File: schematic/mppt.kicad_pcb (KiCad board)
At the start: 2 copper layers, 25 parts, among them J1 Solar, J10 ACS712-OUT, J11 LiIon-36V, J12 Download, J2 TL494-IN, J3 LM2596-IN, J4 LM2596-IN, J5 Serial, J6 LM2596-OUT-4,5V, J7 LM2596-OUT-3,3V, J8 ACS712-IN, J9 TL494-OUT-42V-3A, U3 ESP-03, U4 74HC4051

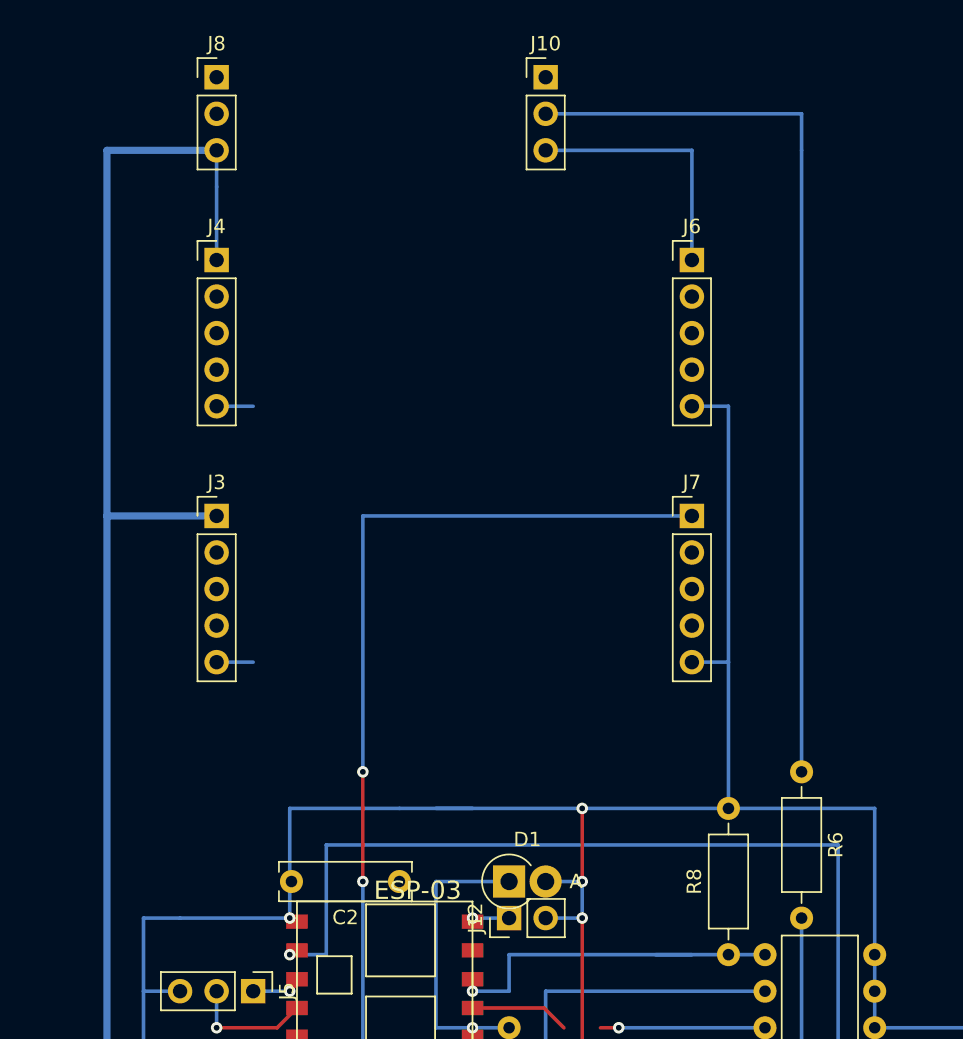
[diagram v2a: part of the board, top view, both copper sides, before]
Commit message: schematic: Use INA219
Signed-off-by: Timo Wischer <twischer@freenet.de>
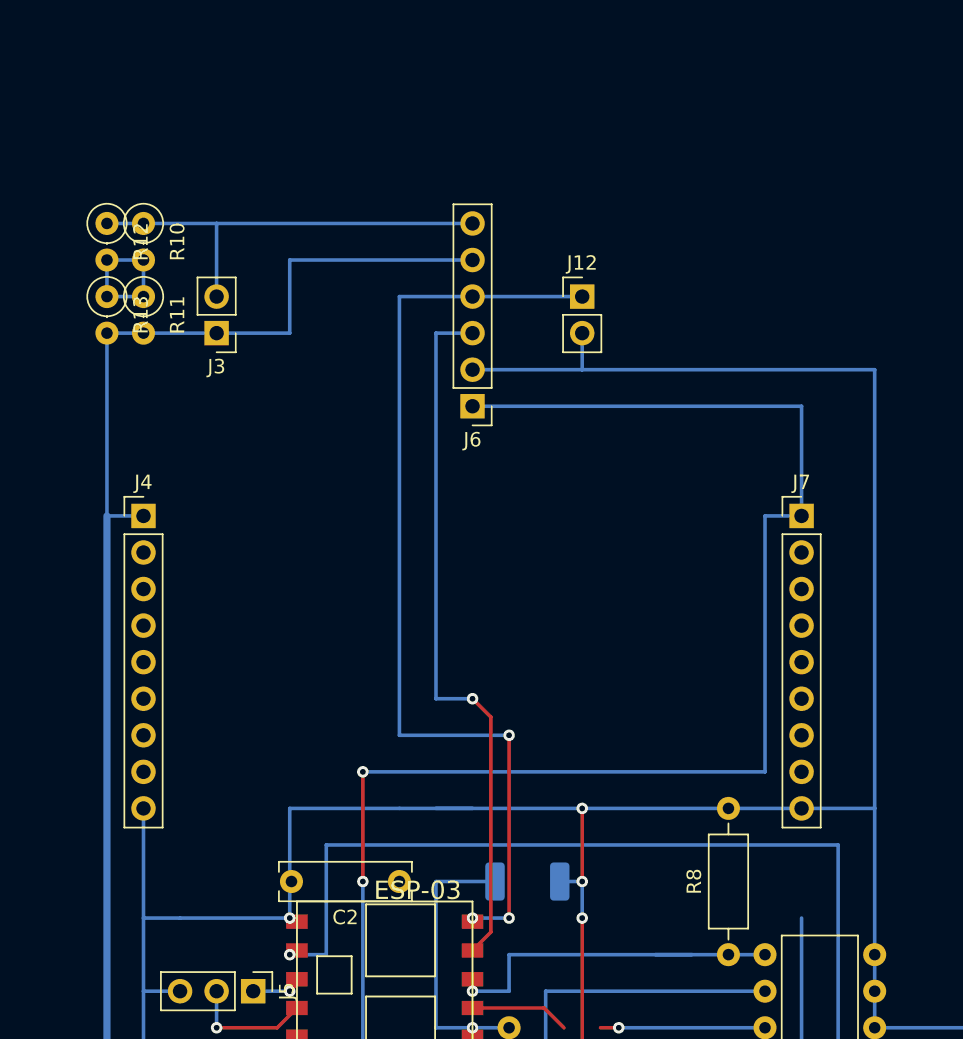
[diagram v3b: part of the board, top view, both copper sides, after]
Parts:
- removed J10: ACS712-OUT, Connector_PinHeader_2.54mm:PinHeader_1x03_P2.54mm_Vertical
- removed J8: ACS712-IN, Connector_PinHeader_2.54mm:PinHeader_1x03_P2.54mm_Vertical
- removed R6: 5k6, Resistor_THT:R_Axial_DIN0207_L6.3mm_D2.5mm_P10.16mm_Horizontal
- added R10: 0,005, Resistor_THT:R_Axial_DIN0207_L6.3mm_D2.5mm_P2.54mm_Vertical, F.Cu at (55.9, 71.1)
- added R11: 0,005, Resistor_THT:R_Axial_DIN0207_L6.3mm_D2.5mm_P2.54mm_Vertical, F.Cu at (55.9, 76.2)
- added R12: 0,005, Resistor_THT:R_Axial_DIN0207_L6.3mm_D2.5mm_P2.54mm_Vertical, F.Cu at (53.3, 71.1)
- added R13: 0,005, Resistor_THT:R_Axial_DIN0207_L6.3mm_D2.5mm_P2.54mm_Vertical, F.Cu at (53.3, 76.2)
- D1: footprint Diode_THT:D_DO-15_P2.54mm_Vertical_AnodeUp -> Diode_SMD:D_2010_5025Metric; moved to B.Cu
- J3: value LM2596-IN -> INA219; footprint Connector_PinHeader_2.54mm:PinHeader_1x05_P2.54mm_Vertical -> Connector_PinHeader_2.54mm:PinHeader_1x02_P2.54mm_Vertical
- J4: footprint Connector_PinHeader_2.54mm:PinHeader_1x05_P2.54mm_Vertical -> Connector_PinHeader_2.54mm:PinHeader_1x09_P2.54mm_Vertical
- J6: value LM2596-OUT-4,5V -> INA219; footprint Connector_PinHeader_2.54mm:PinHeader_1x05_P2.54mm_Vertical -> Connector_PinHeader_2.54mm:PinHeader_1x06_P2.54mm_Vertical
- J7: value LM2596-OUT-3,3V -> LM2596-OUT; footprint Connector_PinHeader_2.54mm:PinHeader_1x05_P2.54mm_Vertical -> Connector_PinHeader_2.54mm:PinHeader_1x09_P2.54mm_Vertical
- moved J12 43.5 mm to (86.4, 76.2), turned to 0 degrees
- moved J4 18.5 mm to (55.9, 91.4)
- moved J6 18.3 mm to (78.7, 83.8), turned to 180 degrees
- moved J3 12.7 mm to (61.0, 78.7), turned to 180 degrees
- moved J7 7.62 mm to (101.6, 91.4)
- moved D1 1.27 mm to (82.5, 116.8)
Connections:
- J3 pad 2: (no net) -> Net-(J1-Pad2)
- J4 pad 5: GND -> (no net)
- J6 pad 1: Net-(J10-Pad3) -> Net-(C2-Pad1)
- J6 pad 2: (no net) -> GND
- J6 pad 3: (no net) -> Net-(J6-Pad3)
- J6 pad 4: (no net) -> Net-(J12-Pad1)
- J6 pad 5: GND -> Net-(J2-Pad1)
- J7 pad 5: GND -> (no net)
- U3 pad 13: (no net) -> Net-(J6-Pad3)
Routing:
- net Net-(J12-Pad1): track 2.79 -> 66.3 mm, vias 1 -> 3
- net Net-(J10-Pad2): track 63.5 -> 0.00 mm
- net Net-(J6-Pad3): track 0.00 -> 49.0 mm, vias 0 -> 1
- net Net-(C2-Pad1): track 112.8 -> 150.9 mm
- net Net-(J1-Pad2): track 0.00 -> 30.5 mm
- net GND: track 239.5 -> 266.4 mm
- net Net-(J10-Pad3): track 17.8 -> 0.00 mm
- net Net-(R10-Pad2): track 0.00 -> 10.2 mm
- net Net-(J2-Pad1): track 172.7 -> 165.1 mm
- net Net-(D1-Pad1): track 20.9 -> 20.0 mm

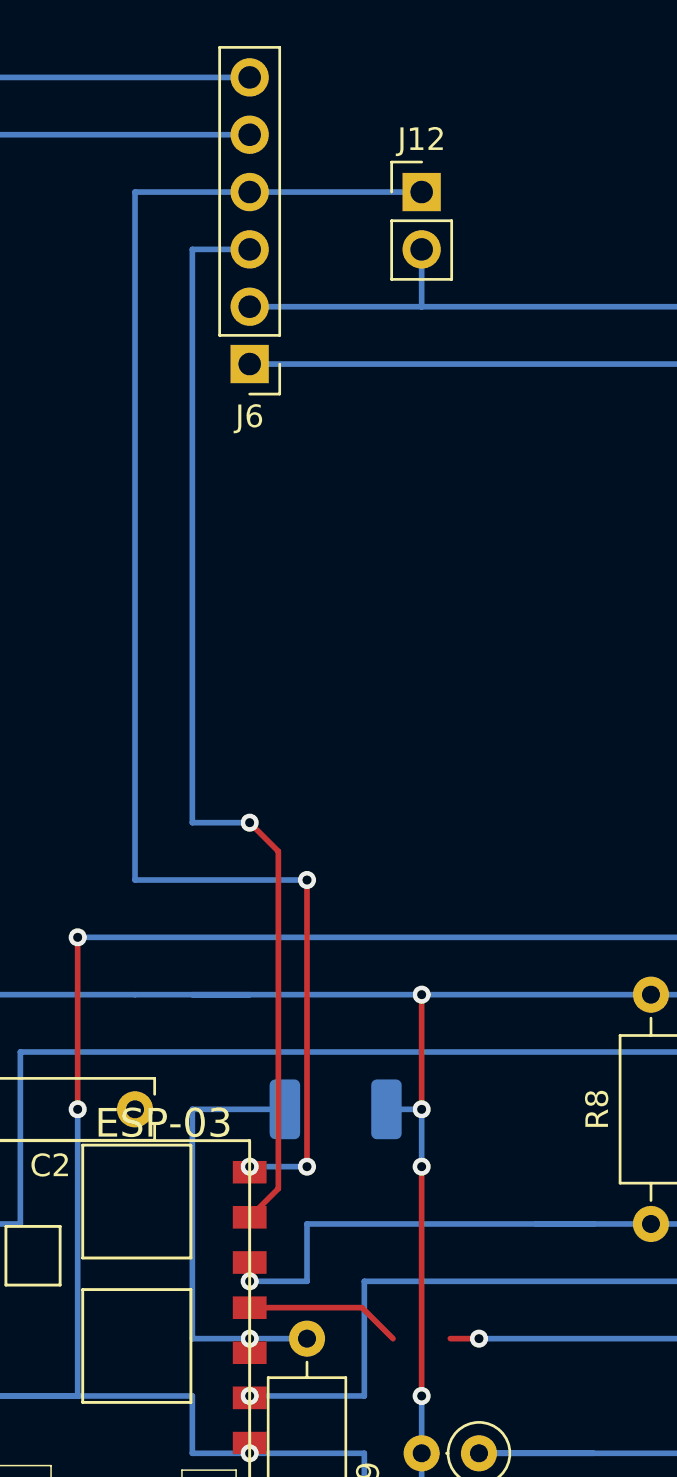
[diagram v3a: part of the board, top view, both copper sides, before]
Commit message: Swap GPIO0 and GPIO13
Signed-off-by: Timo Wischer <twischer@freenet.de>
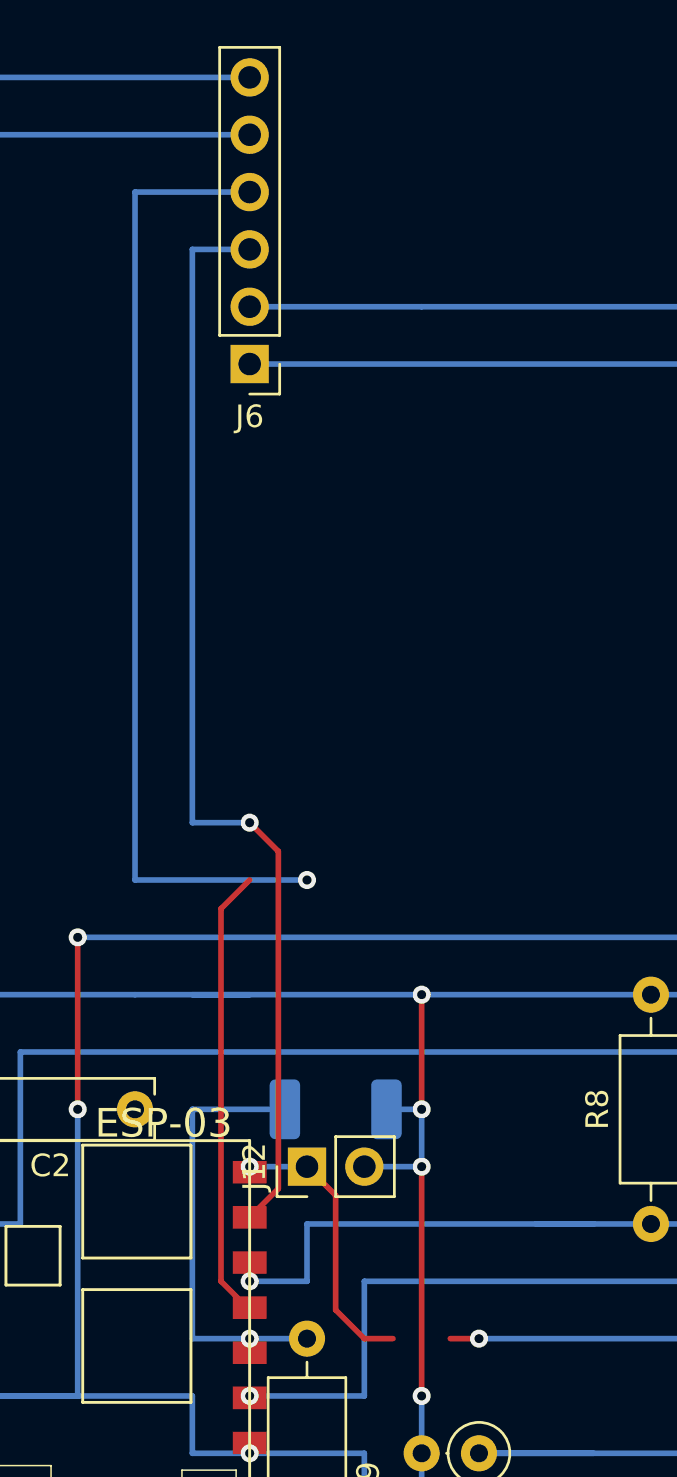
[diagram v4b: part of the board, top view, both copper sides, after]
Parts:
- moved J12 43.5 mm to (81.3, 119.4), turned to 90 degrees
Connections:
- J6 pad 4: Net-(J12-Pad1) -> Net-(J6-Pad4)
- U3 pad 11: Net-(U3-Pad11) -> Net-(J6-Pad4)
- U4 pad 11: Net-(U3-Pad11) -> Net-(J12-Pad1)
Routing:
- net Net-(J6-Pad4): track 0.00 -> 63.2 mm, vias 0 -> 1
- net Net-(J12-Pad1): track 66.3 -> 24.2 mm, vias 3 -> 2
- net Net-(U3-Pad11): track 18.3 -> 0.00 mm, vias 1 -> 0

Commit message: schematic: Reduce GPIO15 pull down to 2,2kOhm
Signed-off-by: Timo Wischer <twischer@freenet.de>
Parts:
- R8: value 10k -> 2k2
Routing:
- net Net-(C1-Pad2): track 0.00 -> 2.54 mm
- net (no net): track 2.54 -> 0.00 mm

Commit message: Update to KiCad 6.0
Signed-off-by: Timo Wischer <twischer@freenet.de>
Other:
- net class Default removed

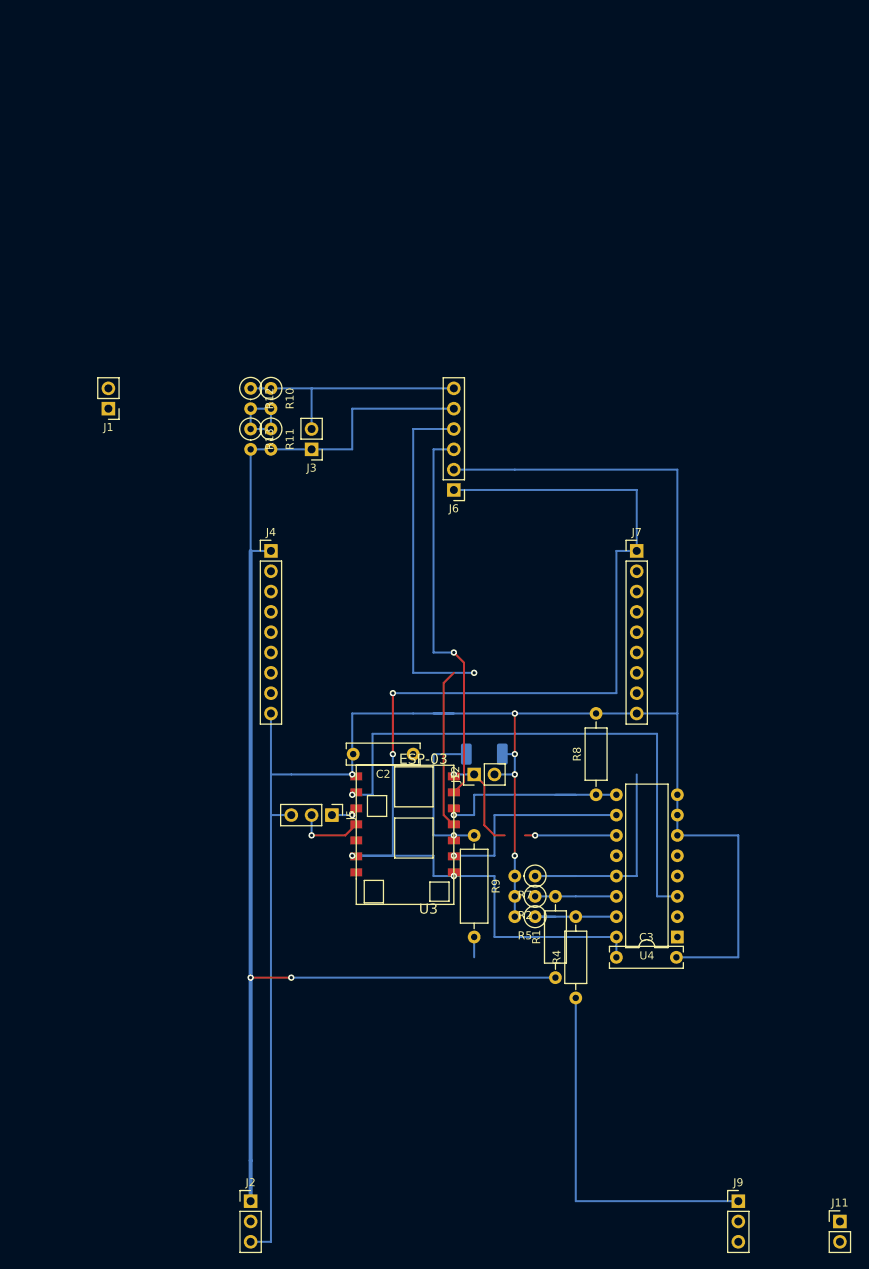
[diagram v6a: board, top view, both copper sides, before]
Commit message: sch: Use error amp of TL494 for MPPT
Signed-off-by: Timo Wischer <twischer@freenet.de>
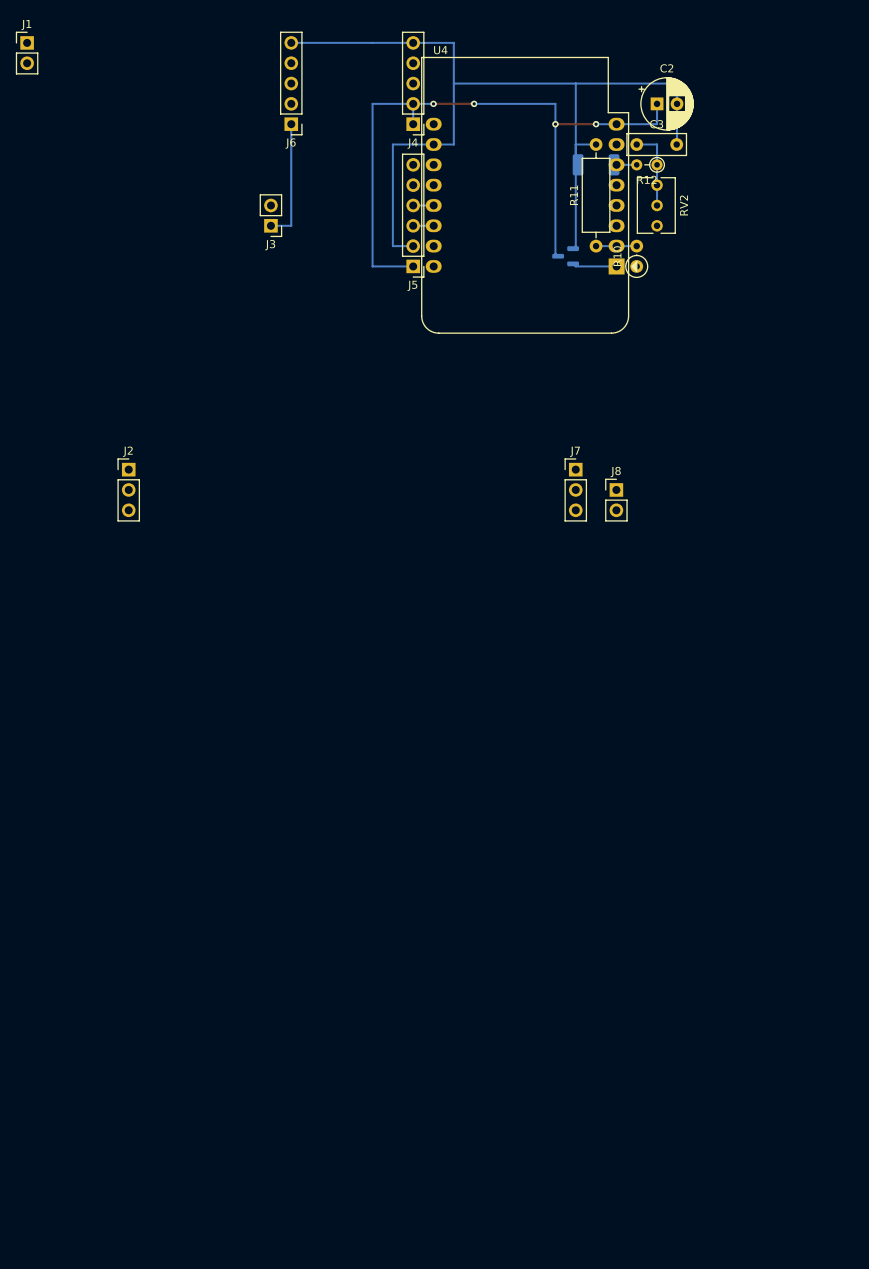
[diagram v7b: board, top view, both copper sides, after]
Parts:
- removed J11: LiIon-36V, Connector_PinHeader_2.54mm:PinHeader_1x02_P2.54mm_Vertical
- removed J12: Download, Connector_PinHeader_2.54mm:PinHeader_1x02_P2.54mm_Vertical
- removed J9: TL494-OUT-42V-3A, Connector_PinHeader_2.54mm:PinHeader_1x03_P2.54mm_Vertical
- removed R1: 56k, Resistor_THT:R_Axial_DIN0207_L6.3mm_D2.5mm_P10.16mm_Horizontal
- removed R13: 0,005, Resistor_THT:R_Axial_DIN0207_L6.3mm_D2.5mm_P2.54mm_Vertical
- removed R2, R5, R7: 2k2, Resistor_THT:R_Axial_DIN0207_L6.3mm_D2.5mm_P2.54mm_Vertical
- removed R4: 120k, Resistor_THT:R_Axial_DIN0207_L6.3mm_D2.5mm_P10.16mm_Horizontal
- removed R8: 2k2, Resistor_THT:R_Axial_DIN0207_L6.3mm_D2.5mm_P10.16mm_Horizontal
- removed R9: 1k2, Resistor_THT:R_Axial_DIN0309_L9.0mm_D3.2mm_P12.70mm_Horizontal
- added J8: LiIon-36V, Connector_PinHeader_2.54mm:PinHeader_1x02_P2.54mm_Vertical, F.Cu at (99.1, 83.8)
- added RV2: 10k, Potentiometer_THT:Potentiometer_Bourns_3266Y_Vertical, F.Cu at (104.1, 50.8)
- C2: value 100n -> 100µ; footprint Capacitor_THT:C_Rect_L9.0mm_W2.5mm_P7.50mm_MKT -> Capacitor_THT:CP_Radial_D6.3mm_P2.50mm
- C3: value 100n -> 1µ; footprint Capacitor_THT:C_Rect_L9.0mm_W2.5mm_P7.50mm_MKT -> Capacitor_THT:C_Rect_L7.2mm_W2.5mm_P5.00mm_FKS2_FKP2_MKS2_MKP2
- J4: value LM2596-IN -> MP2307-OUT; footprint Connector_PinHeader_2.54mm:PinHeader_1x09_P2.54mm_Vertical -> Connector_PinHeader_2.54mm:PinHeader_1x05_P2.54mm_Vertical
- J5: value Serial -> INA219; footprint Connector_PinHeader_2.54mm:PinHeader_1x03_P2.54mm_Vertical -> Connector_PinHeader_2.54mm:PinHeader_1x06_P2.54mm_Vertical
- J6: value INA219 -> MP2307-IN; footprint Connector_PinHeader_2.54mm:PinHeader_1x06_P2.54mm_Vertical -> Connector_PinHeader_2.54mm:PinHeader_1x05_P2.54mm_Vertical
- J7: value LM2596-OUT -> TL494-OUT-42V-3A; footprint Connector_PinHeader_2.54mm:PinHeader_1x09_P2.54mm_Vertical -> Connector_PinHeader_2.54mm:PinHeader_1x03_P2.54mm_Vertical
- R10: value 0,005 -> 120k
- R11: value 0,005 -> 2k2; footprint Resistor_THT:R_Axial_DIN0207_L6.3mm_D2.5mm_P2.54mm_Vertical -> Resistor_THT:R_Axial_DIN0309_L9.0mm_D3.2mm_P12.70mm_Horizontal
- R12: value 0,005 -> 1k2; footprint Resistor_THT:R_Axial_DIN0207_L6.3mm_D2.5mm_P2.54mm_Vertical -> Resistor_THT:R_Axial_DIN0204_L3.6mm_D1.6mm_P2.54mm_Vertical
- U3: value ESP-03 -> MAX809S; footprint ESP8266:ESP-03 -> Package_TO_SOT_SMD:SOT-23; moved to B.Cu
- U4: value 74HC4051 -> WeMos_D1_mini; footprint Package_DIP:DIP-16_W7.62mm -> Module:WEMOS_D1_mini_light
- moved C3 101.6 mm to (101.6, 40.6)
- moved J2 92.7 mm to (38.1, 81.3)
- moved C2 86.8 mm to (104.1, 35.6), turned to 0 degrees
- moved U4 84.2 mm to (99.1, 55.9)
- moved U3 78.5 mm to (92.7, 54.6)
- moved D1 75.0 mm to (96.5, 43.2), turned to 180 degrees
- moved J5 69.3 mm to (73.7, 55.9), turned to 180 degrees
- moved R12 58.0 mm to (104.1, 43.2), turned to 180 degrees
- moved J4 56.2 mm to (73.7, 38.1), turned to 180 degrees
- moved J6 50.0 mm to (58.4, 38.1)
- moved R10 48.2 mm to (101.6, 55.9), turned to 90 degrees
- moved J1 46.8 mm to (25.4, 27.9), turned to 0 degrees
- moved R11 46.6 mm to (96.5, 53.3), turned to 90 degrees
- moved J3 28.4 mm to (55.9, 50.8)
- moved J7 12.7 mm to (94.0, 81.3)
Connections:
- C3 pad 1: Net-(C2-Pad1) -> Net-(C3-Pad1)
- J2 pad 2: (no net) -> unconnected-(J2-Pad2)
- J4 pad 1: Net-(J2-Pad1) -> Net-(C2-Pad1)
- J4 pad 2: (no net) -> Net-(C2-Pad1)
- J4 pad 3: (no net) -> unconnected-(J4-Pad3)
- J4 pad 4: (no net) -> unconnected-(J4-Pad4)
- J4 pad 5: (no net) -> GND
- J5 pad 1: Net-(J5-Pad1) -> Net-(C2-Pad1)
- J5 pad 2: Net-(J5-Pad2) -> GND
- J5 pad 3: GND -> Net-(J5-Pad3)
- J6 pad 1: Net-(C2-Pad1) -> Net-(J2-Pad1)
- J6 pad 2: GND -> unconnected-(J6-Pad2)
- J6 pad 3: Net-(J6-Pad3) -> unconnected-(J6-Pad3)
- J6 pad 4: Net-(J6-Pad4) -> unconnected-(J6-Pad4)
- J6 pad 5: Net-(J2-Pad1) -> GND
- J7 pad 1: Net-(C2-Pad1) -> Net-(F1-Pad2)
- J7 pad 2: (no net) -> unconnected-(J7-Pad2)
- J7 pad 3: (no net) -> Net-(J7-Pad3)
- R10 pad 1: Net-(J1-Pad2) -> Net-(F1-Pad2)
- R11 pad 2: Net-(J2-Pad1) -> GND
- R12 pad 1: Net-(J1-Pad2) -> Net-(C3-Pad1)
- R12 pad 2: Net-(R10-Pad2) -> Net-(D1-Pad1)
- U3 pad 3: Net-(J5-Pad1) -> Net-(C2-Pad1)
- U4 pad 1: (no net) -> Net-(U3-Pad2)
- U4 pad 10: Net-(U3-Pad9) -> GND
- U4 pad 11: Net-(J12-Pad1) -> unconnected-(U4-Pad11)
- U4 pad 12: (no net) -> unconnected-(U4-Pad12)
- U4 pad 13: Net-(R7-Pad1) -> Net-(J5-Pad4)
- U4 pad 14: Net-(R1-Pad2) -> Net-(J5-Pad3)
- U4 pad 15: Net-(R4-Pad2) -> unconnected-(U4-Pad15)
- U4 pad 16: Net-(C2-Pad1) -> unconnected-(U4-Pad16)
- U4 pad 2: (no net) -> Net-(R10-Pad2)
- U4 pad 3: Net-(U3-Pad2) -> Net-(C1-Pad2)
- U4 pad 4: (no net) -> unconnected-(U4-Pad4)
- U4 pad 5: (no net) -> unconnected-(U4-Pad5)
- U4 pad 6: GND -> Net-(D1-Pad1)
- U4 pad 7: GND -> unconnected-(U4-Pad7)
- U4 pad 8: GND -> Net-(C2-Pad1)
- U4 pad 9: Net-(R8-Pad1) -> unconnected-(U4-Pad9)
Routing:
- net Net-(J2-Pad1): track 165.1 -> 15.2 mm, vias 2 -> 0
- net GND: track 266.4 -> 117.5 mm, vias 5 -> 0
- net Net-(C2-Pad1): track 150.9 -> 85.2 mm
- net Net-(U3-Pad2): track 69.2 -> 5.57 mm, vias 1 -> 0
- net Net-(J6-Pad4): track 63.2 -> 0.00 mm, vias 1 -> 0
- net Net-(J6-Pad3): track 49.0 -> 0.00 mm, vias 1 -> 0
- net Net-(J11-Pad1): track 45.7 -> 0.00 mm
- net Net-(R7-Pad1): track 30.5 -> 0.00 mm
- net Net-(J1-Pad2): track 30.5 -> 0.00 mm
- net Net-(R8-Pad1): track 26.0 -> 0.00 mm, vias 1 -> 0
- net Net-(U3-Pad9): track 25.7 -> 0.00 mm, vias 1 -> 0
- net Net-(J12-Pad1): track 24.2 -> 0.00 mm, vias 2 -> 0
- net Net-(D1-Pad1): track 20.0 -> 2.52 mm, vias 1 -> 0
- net Net-(R4-Pad2): track 12.7 -> 0.00 mm
- net Net-(C3-Pad1): track 0.00 -> 10.2 mm
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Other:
- rule pad_to_mask_clearance: 0.051 -> 0
